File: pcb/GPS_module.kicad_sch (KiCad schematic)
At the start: 1 part, among them U9 SAM-M10Q-00B

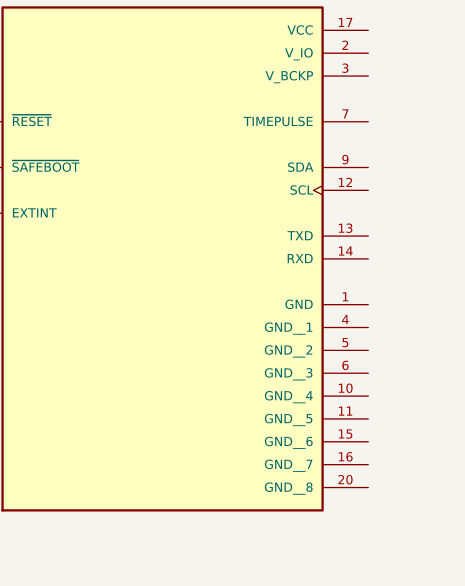
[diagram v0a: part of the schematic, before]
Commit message: Datasheet link attached to footprint
Added datasheet link to footprint and added GND traces.
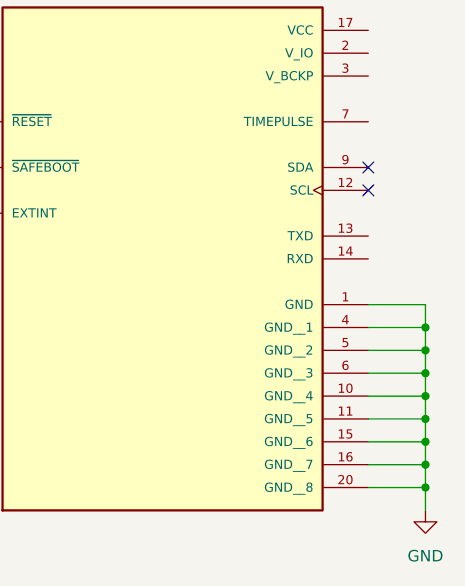
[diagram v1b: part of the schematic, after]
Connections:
- net GND: now reaches U9.1 (GND)
- net GND: now also U9.10 (GND__4), U9.11 (GND__5), U9.15 (GND__6), U9.16 (GND__7), U9.20 (GND__8), U9.4 (GND__1), U9.5 (GND__2), U9.6 (GND__3)
- no-connect marks 0 -> 2

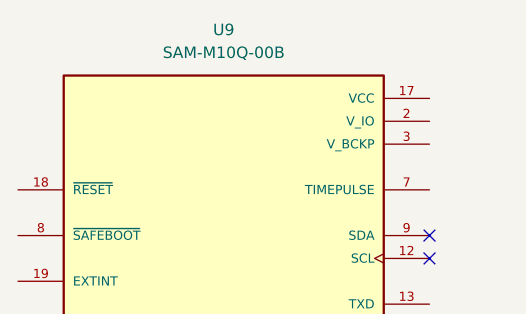
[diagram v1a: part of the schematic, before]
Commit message: Updated schematics and removed most test points
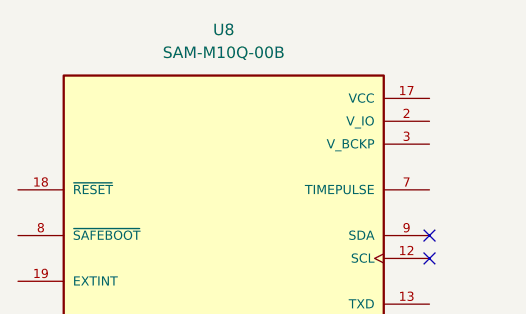
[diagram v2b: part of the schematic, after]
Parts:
- renumbered U9 to U8
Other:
- company: (none) -> Rowan Rocketry
- title: (none) -> Control Module Rev2
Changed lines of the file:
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@@
 	(generator "eeschema")
 	(generator_version "9.0")
-	(paper "A4")
+	(paper "USLetter")
+	(title_block
+		(title "Control Module Rev2")
+		(date "2026-02-10")
+		(rev "2.0")
+		(company "Rowan Rocketry")
+	)
 	(junction
 		(at 170.18 110.49)
@@
 		(dnp no)
 		(fields_autoplaced yes)
-		(property "Reference" "U9"
+		(property "Reference" "U8"
 			(at 140.97 62.23 0)
 			(effects
@@
 			(project "control-module"
 				(path "/ba7b4294-8d75-4b9e-892f-fb52727887ec/fc9e3a2d-4610-4d80-a238-b7d530352ab2"
-					(reference "U9")
+					(reference "U8")
 					(unit 1)
 				)

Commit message: Updated Board layout, finalized dimensions
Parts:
- U8: footprint SAM-M10Q-00B:XCVR_SAM-M10Q-00B -> SAM M10Q:XCVR_SAM-M10Q-00B
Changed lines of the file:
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@@
 			)
 		)
-		(property "Footprint" "SAM-M10Q-00B:XCVR_SAM-M10Q-00B"
+		(property "Footprint" "SAM M10Q:XCVR_SAM-M10Q-00B"
 			(at 140.97 85.09 0)
 			(effects

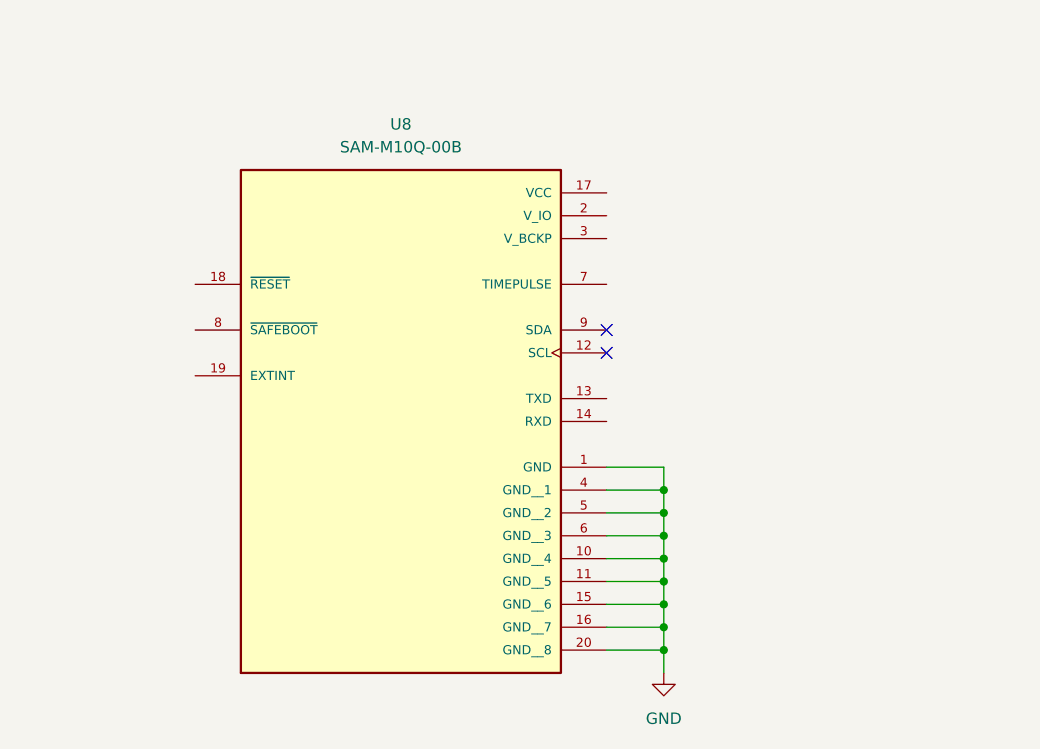
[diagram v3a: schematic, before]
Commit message: Updated Board size and layout
Full Layout of Rev 2 board, without RF shield and other updates.
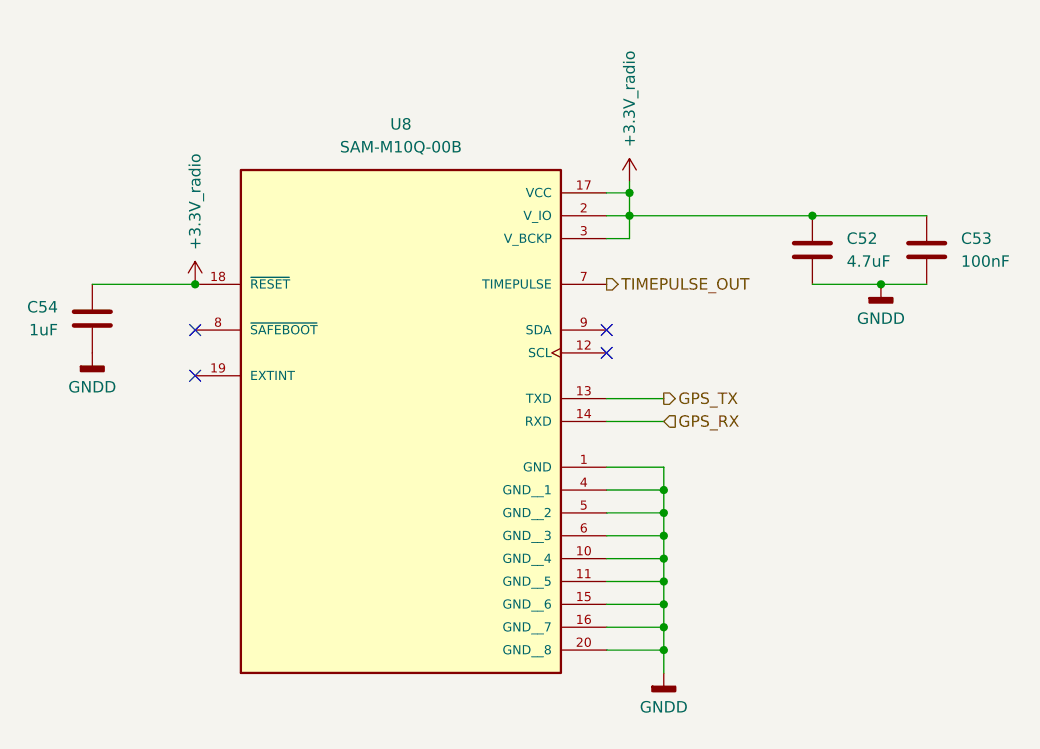
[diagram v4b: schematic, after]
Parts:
- added C52: 4.7uF, Capacitor_SMD:C_0603_1608Metric, symbol Device:C
- added C53: 100nF, Capacitor_SMD:C_0603_1608Metric_Pad1.08x0.95mm_HandSolder, symbol Device:C
- added C54: 1uF, Capacitor_SMD:C_0603_1608Metric_Pad1.08x0.95mm_HandSolder, symbol Device:C
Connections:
- net GPS_TX: now reaches U8.13 (TXD)
- net GPS_RX: now reaches U8.14 (RXD)
- net +3.3V_radio: now reaches U8.17 (VCC)
- net +3.3V_radio: now also U8.18 (~{RESET}), U8.2 (V_IO), U8.3 (V_BCKP), C52.1, C53.1, C54.1
- net TIMEPULSE_OUT: now reaches U8.7 (TIMEPULSE)
- net GND renamed GNDD
- net GNDD: now also C52.2, C53.2, C54.2
- no-connect marks 2 -> 4
